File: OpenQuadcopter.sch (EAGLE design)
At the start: 36 parts, among them U1 MPU-6000QFN-24

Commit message: wrap up openquadcopter board.
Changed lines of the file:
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@@
 <pinref part="U$6" gate="G$1" pin="SOURCE"/>
 <wire x1="22.86" y1="-43.18" x2="22.86" y2="-50.8" width="0.1524" layer="91"/>
+<pinref part="GND3" gate="1" pin="GND"/>
+<pinref part="R3" gate="G$1" pin="1"/>
 <wire x1="22.86" y1="-50.8" x2="30.48" y2="-50.8" width="0.1524" layer="91"/>
-<pinref part="GND3" gate="1" pin="GND"/>
 <junction x="22.86" y="-50.8"/>
-<pinref part="R3" gate="G$1" pin="1"/>
 </segment>
 <segment>
@@
 </segment>
 <segment>
-<pinref part="C12" gate="G$1" pin="2"/>
-<pinref part="GND10" gate="1" pin="GND"/>
-<wire x1="50.8" y1="68.58" x2="50.8" y2="71.12" width="0.1524" layer="91"/>
-<pinref part="U$1" gate="G$1" pin="GND@2"/>
-<wire x1="40.64" y1="88.9" x2="45.72" y2="88.9" width="0.1524" layer="91"/>
-<wire x1="45.72" y1="88.9" x2="45.72" y2="71.12" width="0.1524" layer="91"/>
-<wire x1="45.72" y1="71.12" x2="43.18" y2="71.12" width="0.1524" layer="91"/>
-<wire x1="43.18" y1="71.12" x2="43.18" y2="86.36" width="0.1524" layer="91"/>
-<pinref part="U$1" gate="G$1" pin="GND@1"/>
-<wire x1="43.18" y1="86.36" x2="40.64" y2="86.36" width="0.1524" layer="91"/>
-<wire x1="45.72" y1="71.12" x2="50.8" y2="71.12" width="0.1524" layer="91"/>
-<junction x="45.72" y="71.12"/>
-<junction x="50.8" y="71.12"/>
-</segment>
-<segment>
 <pinref part="C5" gate="G$1" pin="2"/>
 <pinref part="C6" gate="G$1" pin="2"/>
@@
 <junction x="-60.96" y="27.94"/>
 </segment>
+<segment>
+<pinref part="C12" gate="G$1" pin="2"/>
+<pinref part="U$1" gate="G$1" pin="GND@2"/>
+<wire x1="40.64" y1="88.9" x2="45.72" y2="88.9" width="0.1524" layer="91"/>
+<wire x1="45.72" y1="88.9" x2="45.72" y2="71.12" width="0.1524" layer="91"/>
+<wire x1="45.72" y1="71.12" x2="50.8" y2="71.12" width="0.1524" layer="91"/>
+<pinref part="U$1" gate="G$1" pin="GND@1"/>
+<wire x1="40.64" y1="86.36" x2="43.18" y2="86.36" width="0.1524" layer="91"/>
+<wire x1="43.18" y1="86.36" x2="43.18" y2="71.12" width="0.1524" layer="91"/>
+<wire x1="43.18" y1="71.12" x2="45.72" y2="71.12" width="0.1524" layer="91"/>
+<junction x="45.72" y="71.12"/>
+<pinref part="GND10" gate="1" pin="GND"/>
+<wire x1="50.8" y1="71.12" x2="50.8" y2="68.58" width="0.1524" layer="91"/>
+<junction x="50.8" y="71.12"/>
+</segment>
 </net>
 <net name="N$1" class="0">
@@
 </segment>
 <segment>
-<pinref part="U1" gate="G$1" pin="VDD"/>
-<wire x1="-68.58" y1="91.44" x2="-81.28" y2="91.44" width="0.1524" layer="91"/>
-<label x="-81.28" y="91.44" size="1.778" layer="95"/>
-</segment>
-<segment>
-<pinref part="U1" gate="G$1" pin="CS"/>
 <pinref part="P+2" gate="VCC" pin="VCC"/>
-<wire x1="-33.02" y1="91.44" x2="-30.48" y2="91.44" width="0.1524" layer="91"/>
-<wire x1="-30.48" y1="91.44" x2="-30.48" y2="96.52" width="0.1524" layer="91"/>
 <pinref part="U1" gate="G$1" pin="AD0/SDO"/>
 <wire x1="-33.02" y1="86.36" x2="-30.48" y2="86.36" width="0.1524" layer="91"/>
 <wire x1="-30.48" y1="86.36" x2="-30.48" y2="91.44" width="0.1524" layer="91"/>
+<pinref part="U1" gate="G$1" pin="CS"/>
+<wire x1="-30.48" y1="91.44" x2="-30.48" y2="96.52" width="0.1524" layer="91"/>
+<wire x1="-33.02" y1="91.44" x2="-30.48" y2="91.44" width="0.1524" layer="91"/>
 <junction x="-30.48" y="91.44"/>
 </segment>
@@
 <junction x="139.7" y="-10.16"/>
 </segment>
+<segment>
+<pinref part="U1" gate="G$1" pin="VDD"/>
+<wire x1="-68.58" y1="91.44" x2="-81.28" y2="91.44" width="0.1524" layer="91"/>
+<label x="-81.28" y="91.44" size="1.778" layer="95"/>
+</segment>
 </net>
 <net name="MOTOR/PA9" class="0">
@@
 </segment>
 </net>
-<net name="N$13" class="0">
-<segment>
-<pinref part="C11" gate="G$1" pin="1"/>
-<pinref part="U$1" gate="G$1" pin="SETC"/>
-<wire x1="0" y1="88.9" x2="10.16" y2="88.9" width="0.1524" layer="91"/>
-<wire x1="10.16" y1="88.9" x2="10.16" y2="86.36" width="0.1524" layer="91"/>
-</segment>
-</net>
-<net name="N$14" class="0">
-<segment>
-<pinref part="C11" gate="G$1" pin="2"/>
-<pinref part="U$1" gate="G$1" pin="SETP"/>
-<wire x1="0" y1="81.28" x2="10.16" y2="81.28" width="0.1524" layer="91"/>
-<wire x1="10.16" y1="81.28" x2="10.16" y2="83.82" width="0.1524" layer="91"/>
-</segment>
-</net>
 <net name="N$16" class="0">
 <segment>
@@
 </segment>
 </net>
+<net name="N$13" class="0">
+<segment>
+<pinref part="C11" gate="G$1" pin="1"/>
+<wire x1="0" y1="88.9" x2="10.16" y2="88.9" width="0.1524" layer="91"/>
+<pinref part="U$1" gate="G$1" pin="SETC"/>
+<wire x1="10.16" y1="88.9" x2="10.16" y2="86.36" width="0.1524" layer="91"/>
+</segment>
+</net>
+<net name="N$14" class="0">
+<segment>
+<pinref part="U$1" gate="G$1" pin="SETP"/>
+<wire x1="10.16" y1="83.82" x2="10.16" y2="81.28" width="0.1524" layer="91"/>
+<pinref part="C11" gate="G$1" pin="2"/>
+<wire x1="10.16" y1="81.28" x2="0" y2="81.28" width="0.1524" layer="91"/>
+</segment>
+</net>

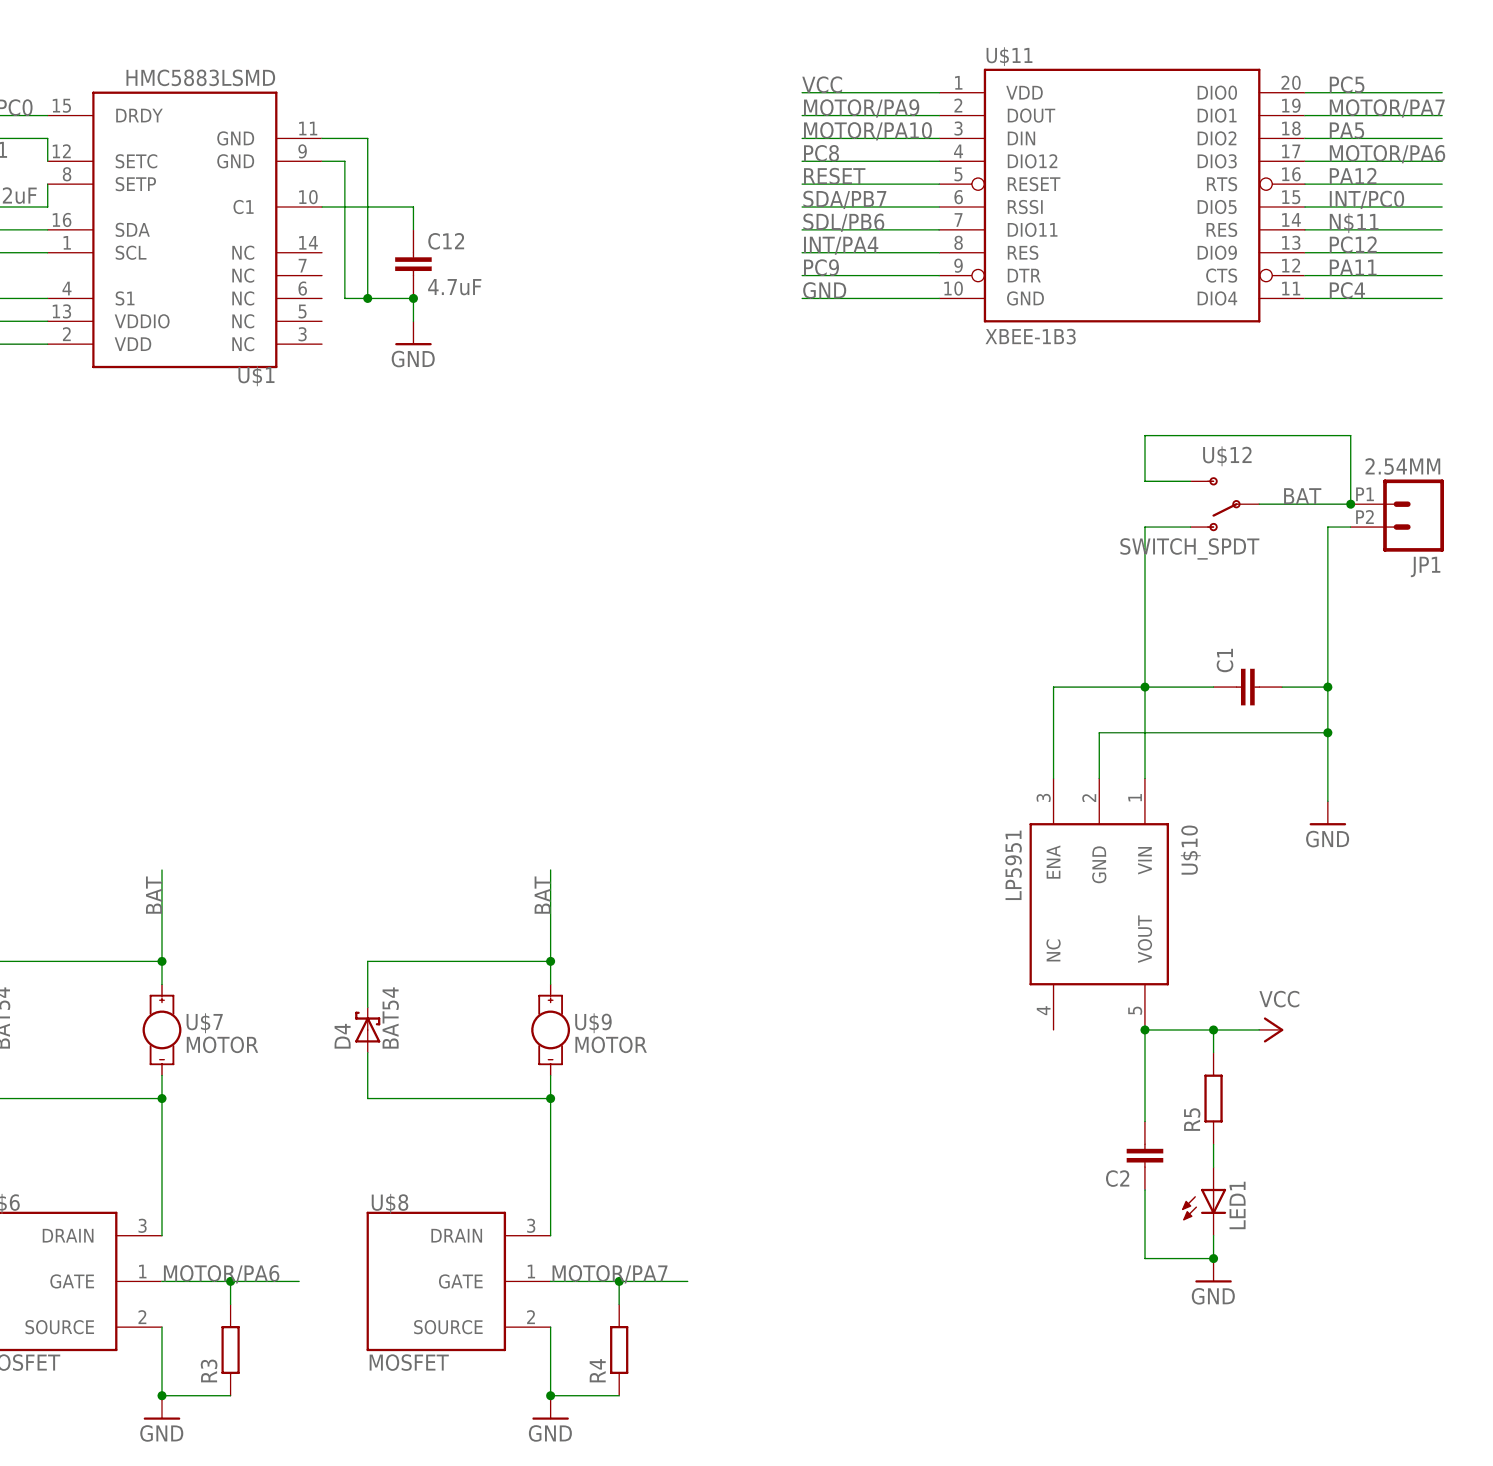
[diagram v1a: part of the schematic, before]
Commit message: Change the PWM's TIM. (Do not use TIM1 for pwm, since the pins are also related to SPI pins)
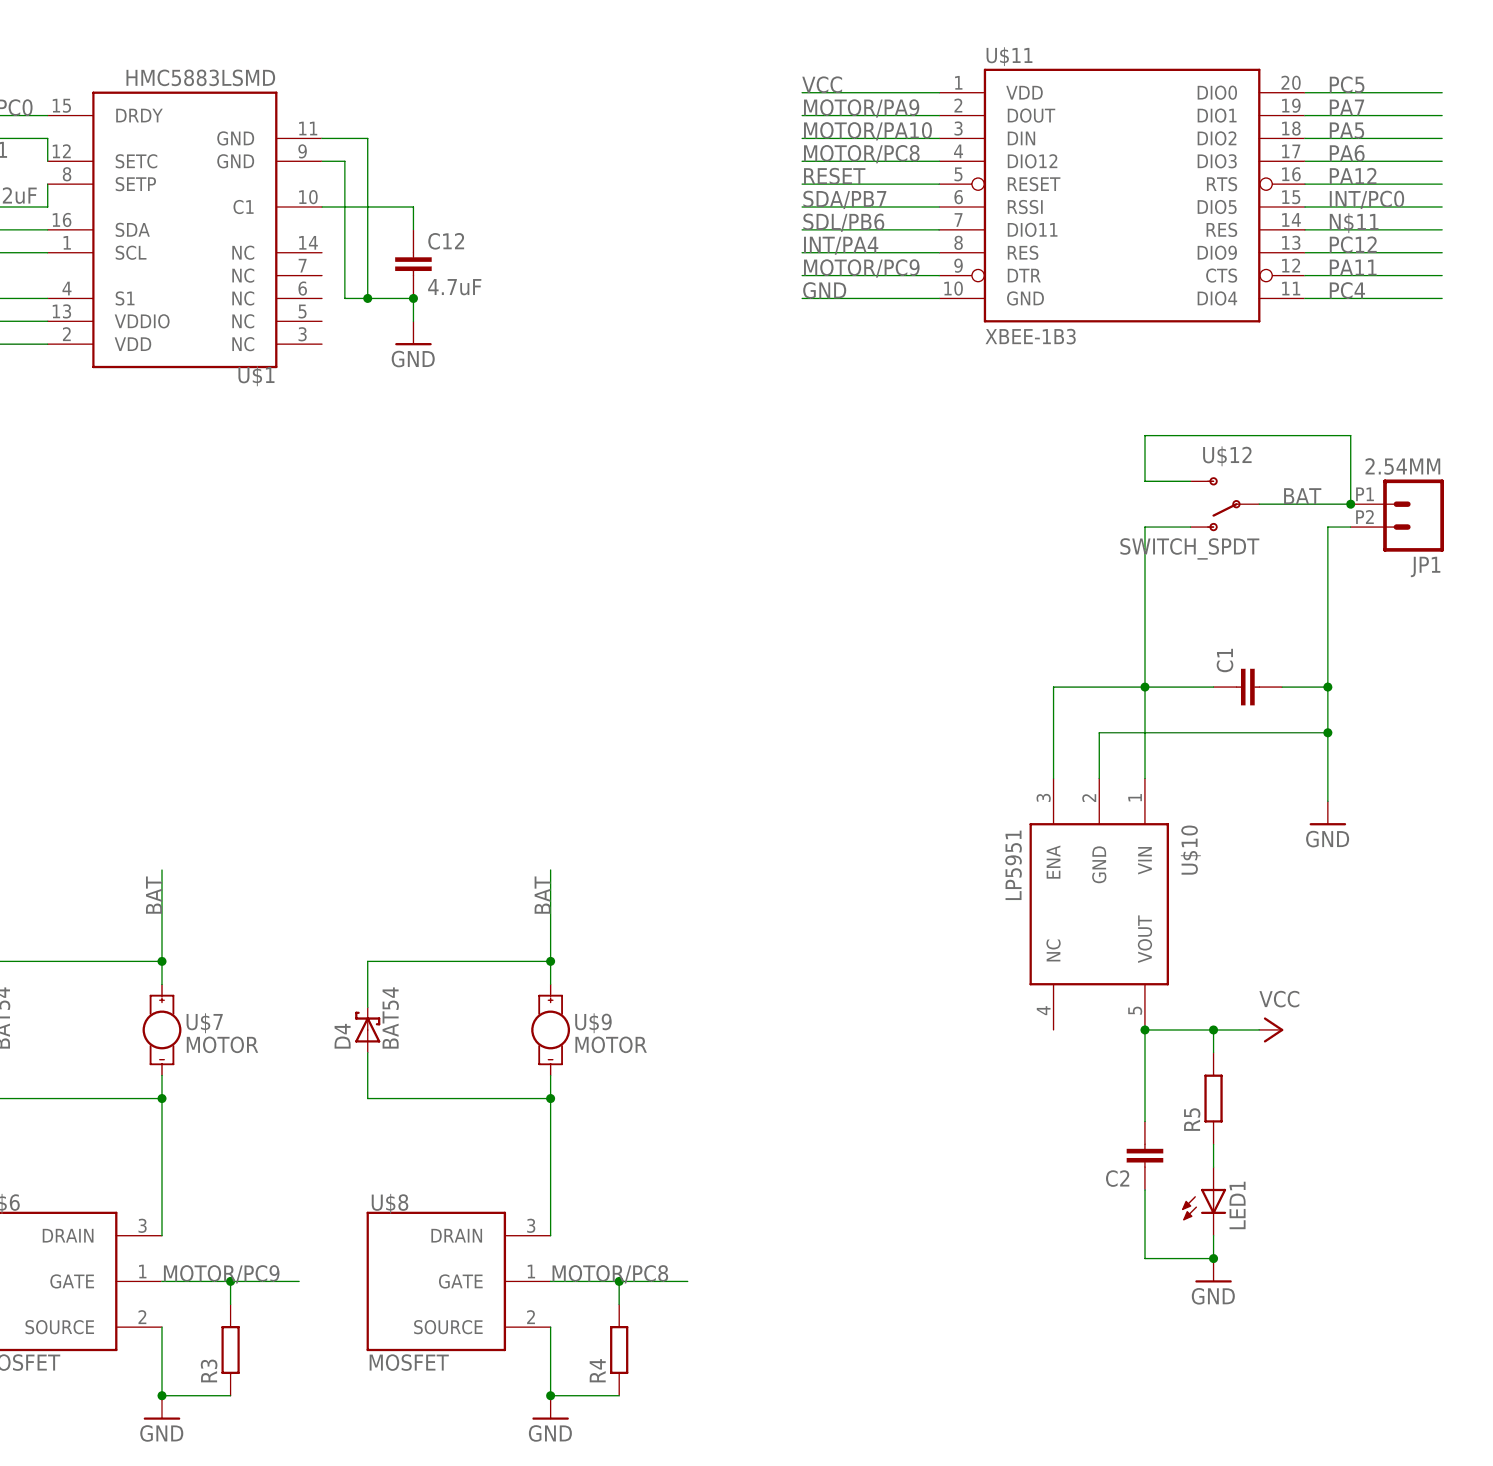
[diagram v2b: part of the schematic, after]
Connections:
- removed net MOTOR/PA6: R3.2, U$11.DIO3, U$6.GATE
- removed net MOTOR/PA7: R4.2, U$11.DIO1, U$8.GATE
- removed net PC8: U$11.DIO12
- removed net PC9: U$11.DTR
- new net MOTOR/PC8: R4.2, U$11.DIO12, U$8.GATE
- new net MOTOR/PC9: R3.2, U$11.DTR, U$6.GATE
- new net PA6: U$11.DIO3
- new net PA7: U$11.DIO1
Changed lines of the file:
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@@
 </segment>
 </net>
-<net name="PC8" class="0">
+<net name="MOTOR/PC8" class="0">
 <segment>
 <pinref part="U$11" gate="G$1" pin="DIO12"/>
@@
 <label x="93.98" y="86.36" size="1.778" layer="95"/>
 </segment>
+<segment>
+<pinref part="U$8" gate="G$1" pin="GATE"/>
+<pinref part="R4" gate="G$1" pin="2"/>
+<wire x1="66.04" y1="-38.1" x2="73.66" y2="-38.1" width="0.1524" layer="91"/>
+<wire x1="73.66" y1="-38.1" x2="73.66" y2="-40.64" width="0.1524" layer="91"/>
+<wire x1="73.66" y1="-38.1" x2="81.28" y2="-38.1" width="0.1524" layer="91"/>
+<junction x="73.66" y="-38.1"/>
+<label x="66.04" y="-38.1" size="1.778" layer="95"/>
+</segment>
 </net>
 <net name="RESET" class="0">
@@
 </segment>
 </net>
-<net name="PC9" class="0">
+<net name="MOTOR/PC9" class="0">
 <segment>
 <pinref part="U$11" gate="G$1" pin="DTR"/>
@@
 <label x="93.98" y="73.66" size="1.778" layer="95"/>
 </segment>
+<segment>
+<pinref part="U$6" gate="G$1" pin="GATE"/>
+<pinref part="R3" gate="G$1" pin="2"/>
+<wire x1="30.48" y1="-38.1" x2="30.48" y2="-40.64" width="0.1524" layer="91"/>
+<junction x="30.48" y="-38.1"/>
+<label x="22.86" y="-38.1" size="1.778" layer="95"/>
+<wire x1="30.48" y1="-38.1" x2="22.86" y2="-38.1" width="0.1524" layer="91"/>
+<wire x1="30.48" y1="-38.1" x2="38.1" y2="-38.1" width="0.1524" layer="91"/>
+</segment>
 </net>
 <net name="PC5" class="0">
@@
 </segment>
 </net>
-<net name="MOTOR/PA7" class="0">
-<segment>
-<pinref part="U$11" gate="G$1" pin="DIO1"/>
-<wire x1="149.86" y1="91.44" x2="165.1" y2="91.44" width="0.1524" layer="91"/>
-<label x="152.4" y="91.44" size="1.778" layer="95"/>
-</segment>
-<segment>
-<pinref part="U$8" gate="G$1" pin="GATE"/>
-<wire x1="66.04" y1="-38.1" x2="73.66" y2="-38.1" width="0.1524" layer="91"/>
-<wire x1="73.66" y1="-38.1" x2="81.28" y2="-38.1" width="0.1524" layer="91"/>
-<wire x1="73.66" y1="-40.64" x2="73.66" y2="-38.1" width="0.1524" layer="91"/>
-<junction x="73.66" y="-38.1"/>
-<pinref part="R4" gate="G$1" pin="2"/>
-<label x="66.04" y="-38.1" size="1.778" layer="95"/>
-</segment>
-</net>
 <net name="PA5" class="0">
 <segment>
@@
 <wire x1="149.86" y1="88.9" x2="165.1" y2="88.9" width="0.1524" layer="91"/>
 <label x="152.4" y="88.9" size="1.778" layer="95"/>
-</segment>
-</net>
-<net name="MOTOR/PA6" class="0">
-<segment>
-<pinref part="U$11" gate="G$1" pin="DIO3"/>
-<wire x1="149.86" y1="86.36" x2="165.1" y2="86.36" width="0.1524" layer="91"/>
-<label x="152.4" y="86.36" size="1.778" layer="95"/>
-</segment>
-<segment>
-<pinref part="U$6" gate="G$1" pin="GATE"/>
-<wire x1="22.86" y1="-38.1" x2="30.48" y2="-38.1" width="0.1524" layer="91"/>
-<wire x1="30.48" y1="-38.1" x2="38.1" y2="-38.1" width="0.1524" layer="91"/>
-<wire x1="30.48" y1="-40.64" x2="30.48" y2="-38.1" width="0.1524" layer="91"/>
-<junction x="30.48" y="-38.1"/>
-<pinref part="R3" gate="G$1" pin="2"/>
-<label x="22.86" y="-38.1" size="1.778" layer="95"/>
 </segment>
 </net>
@@
 </segment>
 </net>
+<net name="PA7" class="0">
+<segment>
+<pinref part="U$11" gate="G$1" pin="DIO1"/>
+<wire x1="149.86" y1="91.44" x2="165.1" y2="91.44" width="0.1524" layer="91"/>
+<label x="152.4" y="91.44" size="1.778" layer="95"/>
+</segment>
+</net>
+<net name="PA6" class="0">
+<segment>
+<pinref part="U$11" gate="G$1" pin="DIO3"/>
+<wire x1="149.86" y1="86.36" x2="165.1" y2="86.36" width="0.1524" layer="91"/>
+<label x="152.4" y="86.36" size="1.778" layer="95"/>
+</segment>
+</net>

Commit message: update openquadcopter.
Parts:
- removed LED1: (no value), led:LEDCHIP-LED0603
- added D5: GREEN, openmotestm:LED-GREEN0603
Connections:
- removed net MOTOR/PA10: R2.2, U$11.DIN, U$4.GATE
- removed net MOTOR/PA9: R1.2, U$11.DOUT, U$2.GATE
- removed net N$15: LED1.A, R5.1
- removed net PA6: U$11.DIO3
- removed net PA7: U$11.DIO1
- new net MOTOR/PA6: R3.2, U$11.DIO3, U$6.GATE
- new net MOTOR/PA7: R4.2, U$11.DIO1, U$8.GATE
- new net N$17: D5.A, R5.1
- new net PA10: U$11.DIN
- new net PA9: U$11.DOUT
- net GND: now also D5.C; no longer LED1.C
- net MOTOR/PC8: now also R1.2, U$2.GATE; no longer R4.2, U$8.GATE
- net MOTOR/PC9: now also R2.2, U$4.GATE; no longer R3.2, U$6.GATE
